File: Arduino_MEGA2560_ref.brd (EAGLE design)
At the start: 101.6 x 45.7 mm, 74 parts, among them IC1 7805DT, IC2 7805DT, T1 PHT8N06LTSOT223, T2 PHT8N06LTSOT223, T3 PHT8N06LTSOT223, T4 PHT8N06LTSOT223, T5 PHT8N06LTSOT223, T6 PHT8N06LTSOT223, X1 MKDSN1,5/2-5,08, X2 MKDSN1,5/2-5,08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

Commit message: doing moving
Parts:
- moved C1 10.4 mm to (17.9, 54.1), turned to 270 degrees
- moved R11 6.61 mm to (108.7, 0.89), turned to 270 degrees
- moved C3 6.20 mm to (9.78, 34.2), turned to 180 degrees
- moved R12 4.95 mm to (107.2, -3.94), turned to 0 degrees
- moved IC1 4.15 mm to (6.35, 29.0), turned to 90 degrees
- moved R7 2.74 mm to (88.9, -4.70)
- moved R9 2.32 mm to (75.3, -3.43), turned to 0 degrees
- moved R13 2.05 mm to (21.2, 56.8)
- moved T4 1.91 mm to (96.5, -9.53)
- moved R14 1.73 mm to (32.6, 60.5), turned to 180 degrees
- moved L3 1.42 mm to (109.9, 63.5)
- moved R8 1.28 mm to (88.9, -10.9)
- moved X13 1.27 mm to (44.1, 65.4)
- moved R21 1.27 mm to (113.0, 59.7), turned to 0 degrees
- moved R2 1.20 mm to (31.4, -2.67), turned to 0 degrees
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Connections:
- net ADC13: no longer R7.1
- net ADC14: now also R7.1; no longer R11.1
- net ADC15: now also R11.1
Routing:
- net GND: track 289.4 -> 144.0 mm
- net +5V: track 260.6 -> 158.7 mm
- net +12V: track 247.6 -> 167.7 mm
- net PB7: track 41.1 -> 0.00 mm
- net PB6: track 26.4 -> 0.00 mm
- net N$4: track 33.0 -> 8.15 mm
- net N$1: track 21.8 -> 0.00 mm
- net ADC15: track 0.00 -> 17.2 mm
- net PB4: track 15.1 -> 0.00 mm
- net PH6: track 14.7 -> 0.51 mm
- net ADC0: track 18.7 -> 5.40 mm
- net ADC14: track 19.4 -> 6.29 mm
- net ADC13: track 7.30 -> 0.00 mm
- net N$8: track 31.7 -> 27.9 mm
- net N$9: track 10.3 -> 7.76 mm
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- added copper zone on layer 1, net +12V
- added copper zone on layer 1, net +5V
- added copper zone on layer 1, net ADC0
- added copper zone on layer 1, net ADC1
- added copper zone on layer 1, net ADC14
- added copper zone on layer 1, net ADC15
- added copper zone on layer 1, net ADC5
- added copper zone on layer 1, net ADC8
- added copper zone on layer 1, net N$1
- added copper zone on layer 1, net N$10
- added copper zone on layer 1, net N$11
- added copper zone on layer 1, net N$12
- added copper zone on layer 1, net N$2
- added copper zone on layer 1, net N$3
- added copper zone on layer 1, net N$4
- added copper zone on layer 1, net N$5
- added copper zone on layer 1, net N$6
- added copper zone on layer 1, net N$7
- added copper zone on layer 1, net N$8
- added copper zone on layer 1, net N$9
- added copper zone on layer 1, net PB4
- added copper zone on layer 1, net PB6
- added copper zone on layer 1, net PB7
- added copper zone on layer 1, net PH6
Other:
- board size 101.6 x 45.7 mm -> 114.5 x 85.1 mm

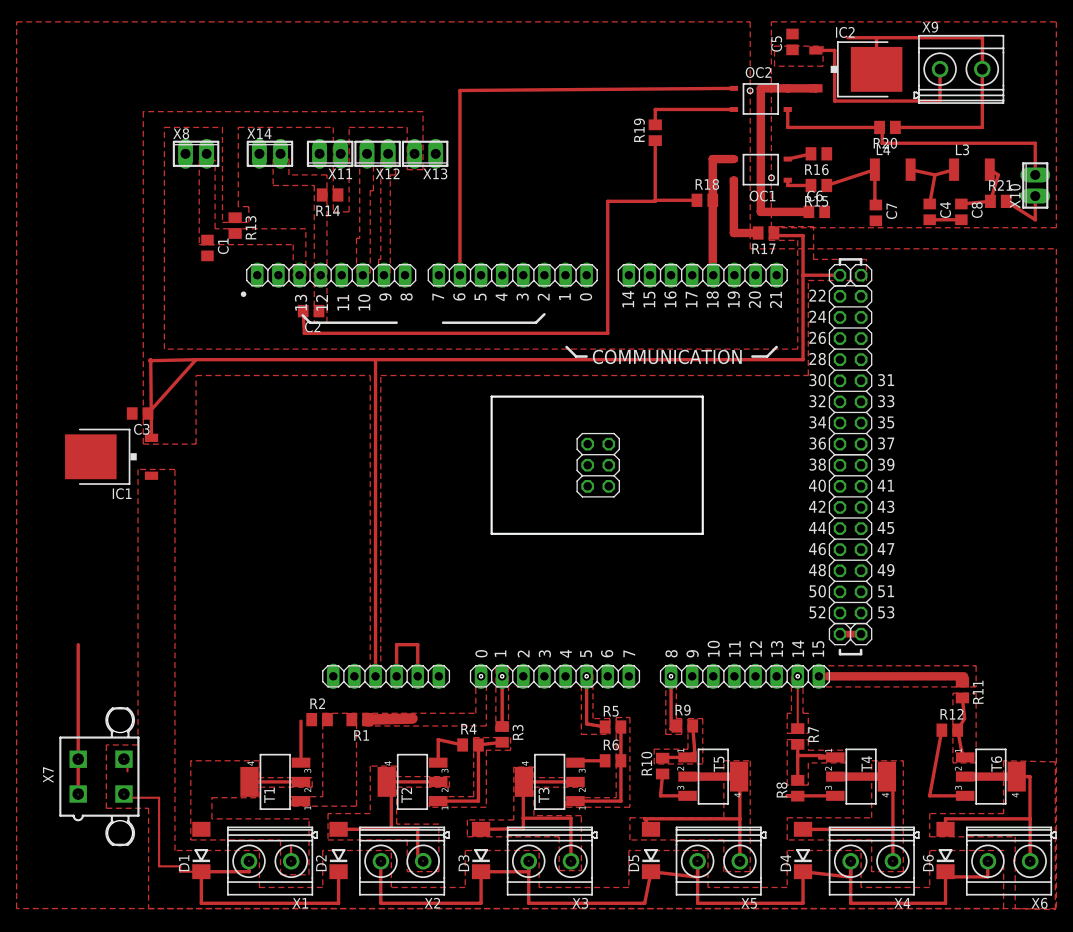
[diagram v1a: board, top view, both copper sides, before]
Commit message: remading AGND
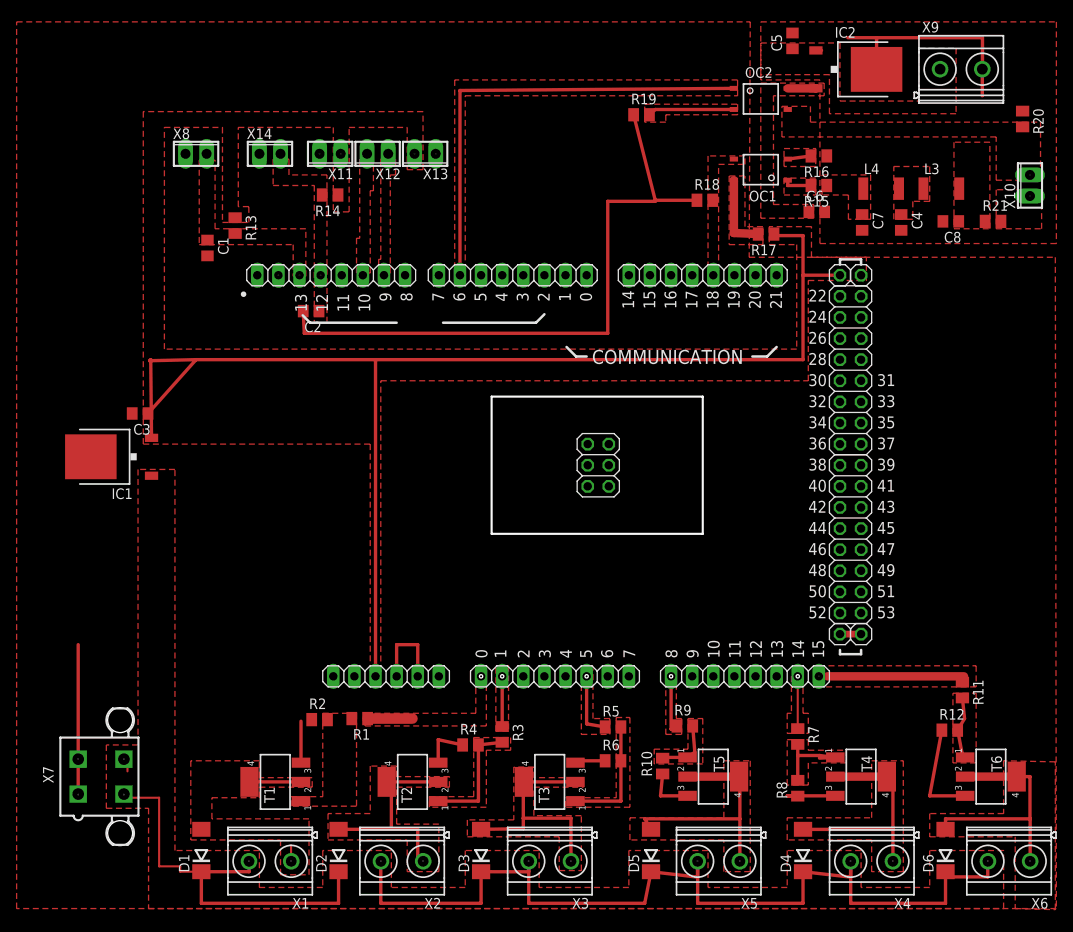
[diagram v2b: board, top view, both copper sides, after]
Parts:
- moved R20 16.3 mm to (116.0, 69.6), turned to 270 degrees
- moved L3 4.33 mm to (106.2, 61.2)
- moved C4 3.66 mm to (101.3, 57.1)
- moved R19 2.72 mm to (70.1, 70.1), turned to 0 degrees
- moved L4 2.68 mm to (98.9, 61.2)
- moved R21 2.50 mm to (112.4, 57.3)
- moved C7 2.01 mm to (96.6, 57.1)
- moved C8 1.71 mm to (107.3, 57.3), turned to 180 degrees
- moved X10 0.63 mm to (116.8, 61.6)
- moved R16 0.25 mm to (91.4, 65.2)
- moved R17 0.13 mm to (85.1, 55.8)
- moved R1 0.13 mm to (36.2, -2.54)
- moved C5 0.13 mm to (88.3, 79.0)
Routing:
- net N$18: track 38.4 -> 0.00 mm
- net +24V: track 25.5 -> 0.68 mm
- net +5V_1: track 27.5 -> 3.65 mm
- net GNDA: track 45.1 -> 27.0 mm
- net TXD1/INT3: track 16.6 -> 0.07 mm
- net N$21: track 10.4 -> 0.00 mm
- net N$20: track 8.93 -> 0.00 mm
- net N$17: track 8.03 -> 0.00 mm
- net N$19: track 7.00 -> 0.00 mm
- net GND: track 144.0 -> 147.4 mm
- net N$16: track 11.3 -> 10.4 mm
- added copper zone on layer 1, net +5V_1
- added copper zone on layer 1, net N$13
- added copper zone on layer 1, net N$14
- added copper zone on layer 1, net N$15
- added copper zone on layer 1, net N$16
- added copper zone on layer 1, net N$17
- added copper zone on layer 1, net N$18
- added copper zone on layer 1, net N$19
- added copper zone on layer 1, net N$20
- added copper zone on layer 1, net N$21
- added copper zone on layer 1, net PH3
- added copper zone on layer 1, net TXD1/INT3
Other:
- outline, holes or cut-outs redrawn
